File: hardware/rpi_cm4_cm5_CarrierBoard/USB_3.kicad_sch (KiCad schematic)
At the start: 92 parts, among them J2 0484050003, J3 0484050003, U6 SST25VF512A, U7 UPD720202K8-711-BAA-A, U8 AP2192AFGEG-7, Y1 24MHz

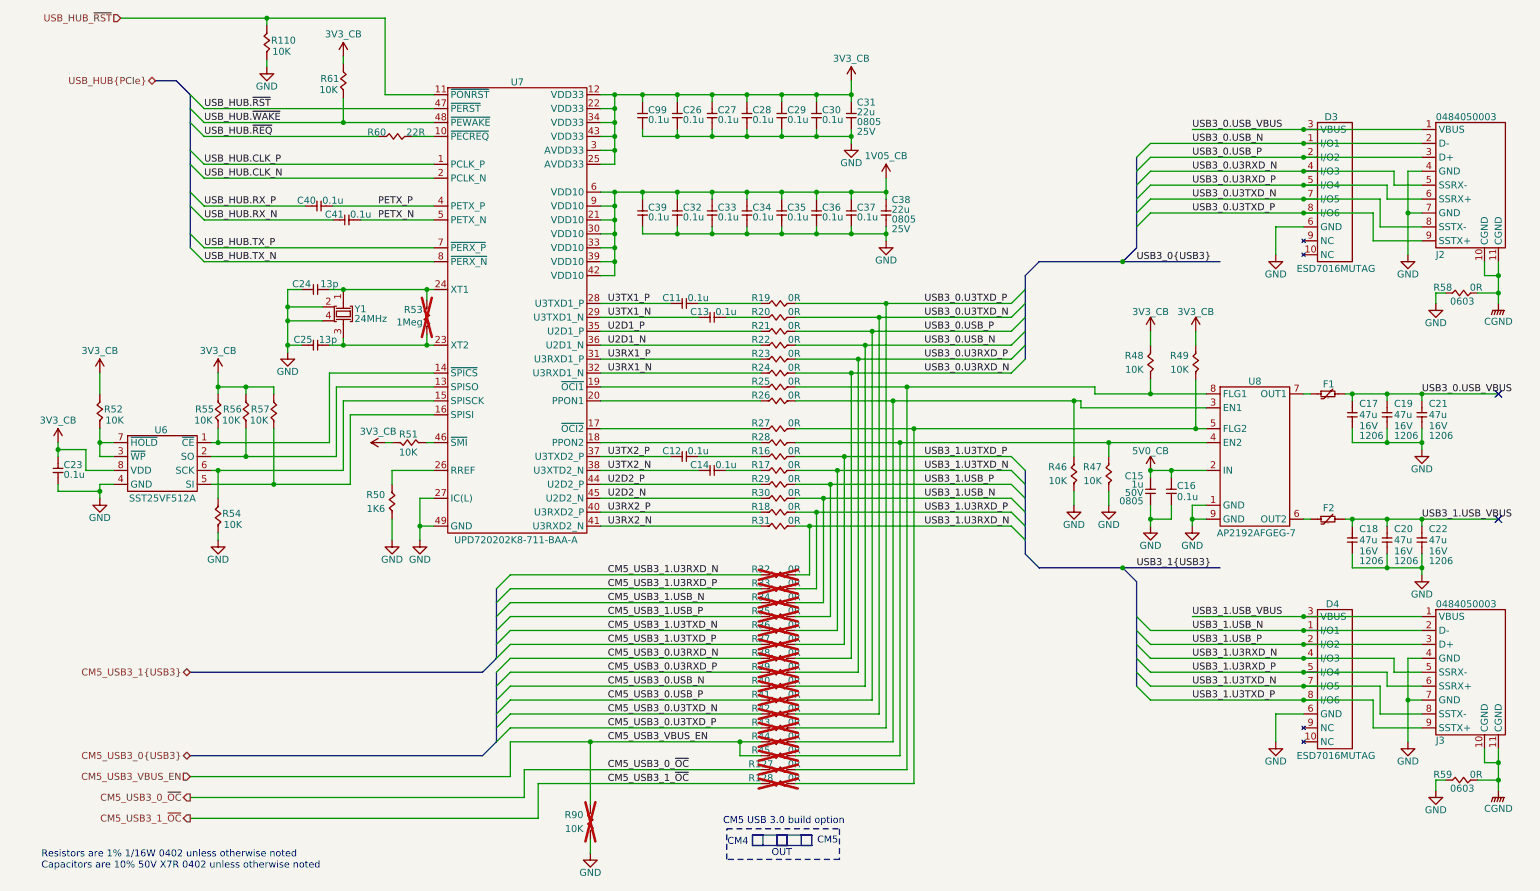
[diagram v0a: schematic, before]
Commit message: Add power-up and power kill sequences Modify schematics to add net classes for DiffPairs
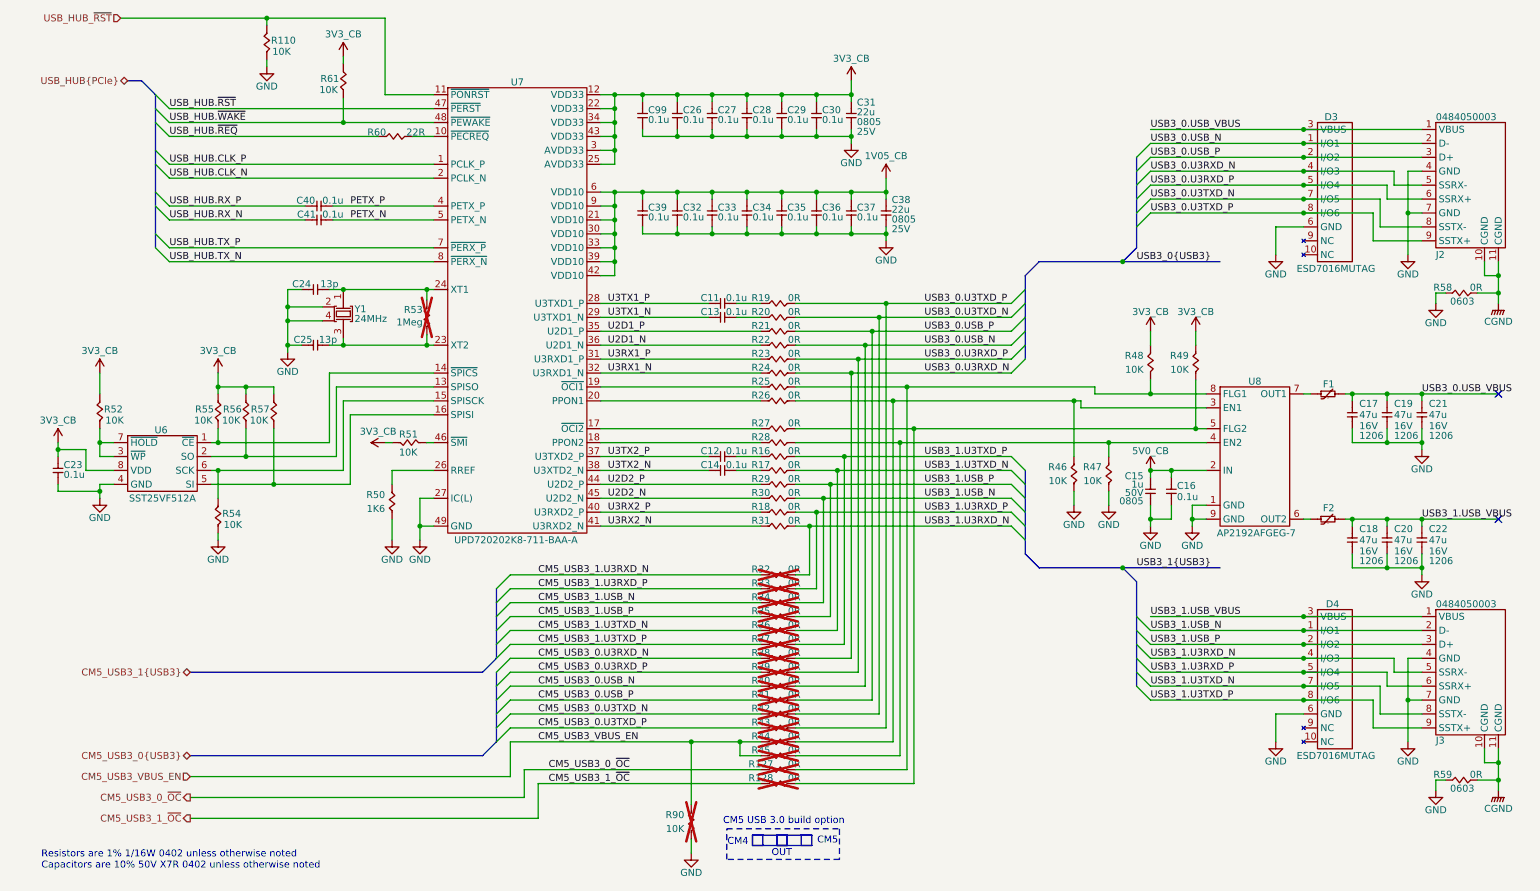
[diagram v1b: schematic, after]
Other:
- moved on the sheet: C11, C12, C13, C14, C41, R90

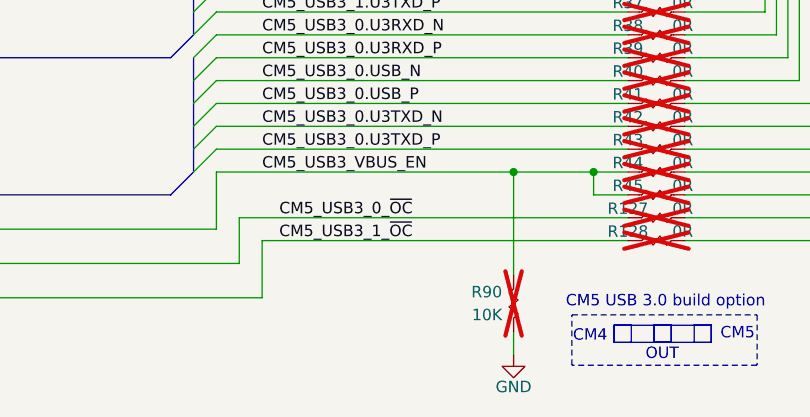
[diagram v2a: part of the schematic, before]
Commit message: Add preliminary BOM and preliminary .pdf schmematics Add BOM option for I2C control of ILI2132A for CapTouch HMI Add BOM options and DNP / 0R resistors for CM4 - CM5 build options
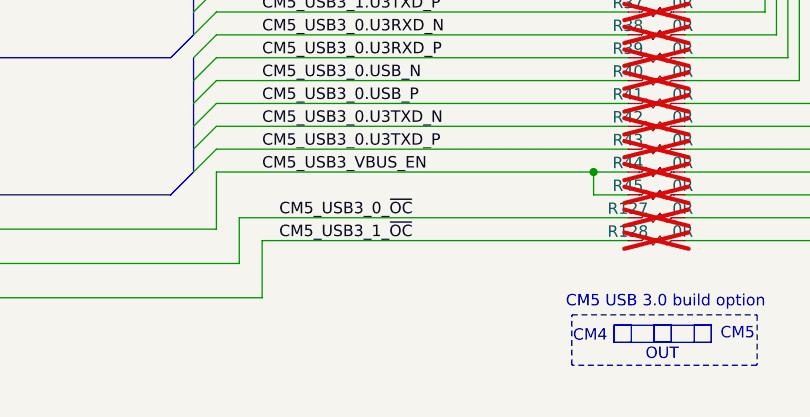
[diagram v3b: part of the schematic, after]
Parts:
- removed R90: 10K, footprint:RES_0402, symbol KicadCompDb:Resistors/RES_SMT_00013

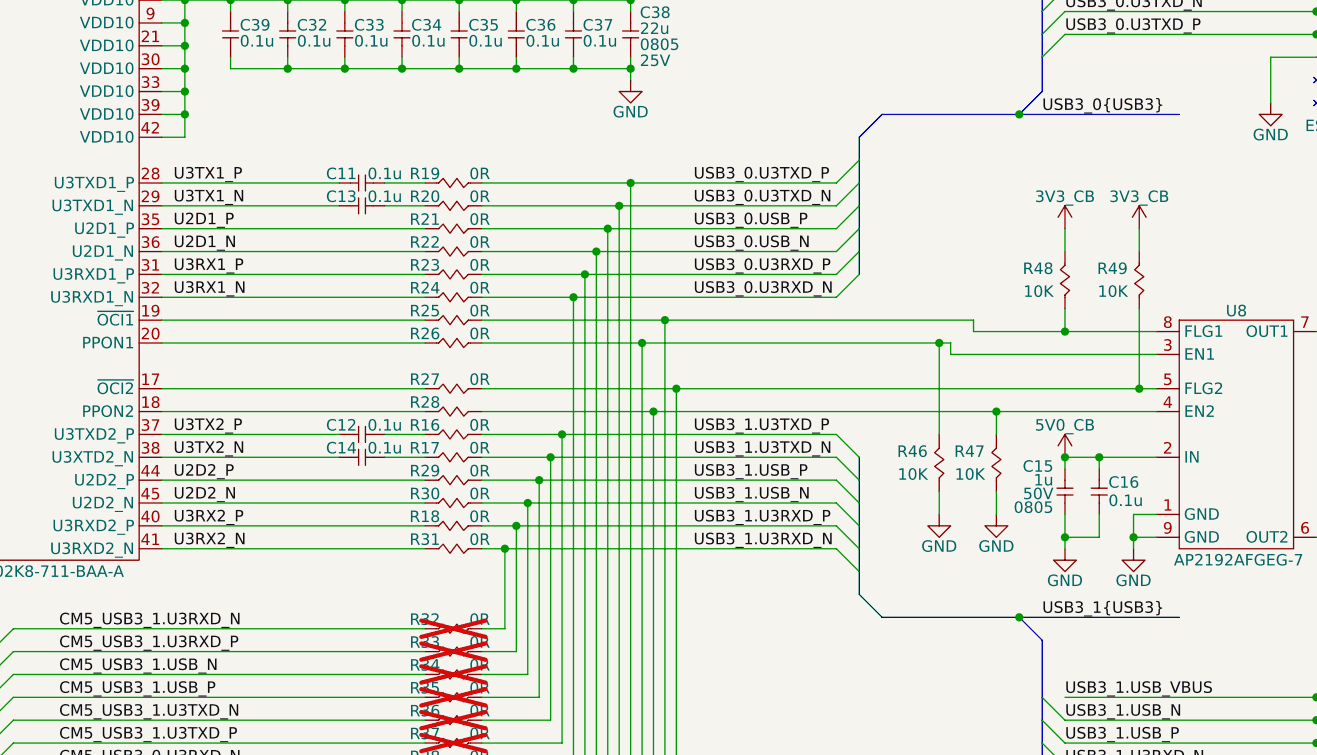
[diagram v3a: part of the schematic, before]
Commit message: Update watchdog timer circuit to add external watchdog timer IC to be fed by PIC Adjust reset scheme in power supply sheet accordingly Adjust PinMux, regen BOM and PDF schematics (preliminary) Start preliminary component placement in the PCB
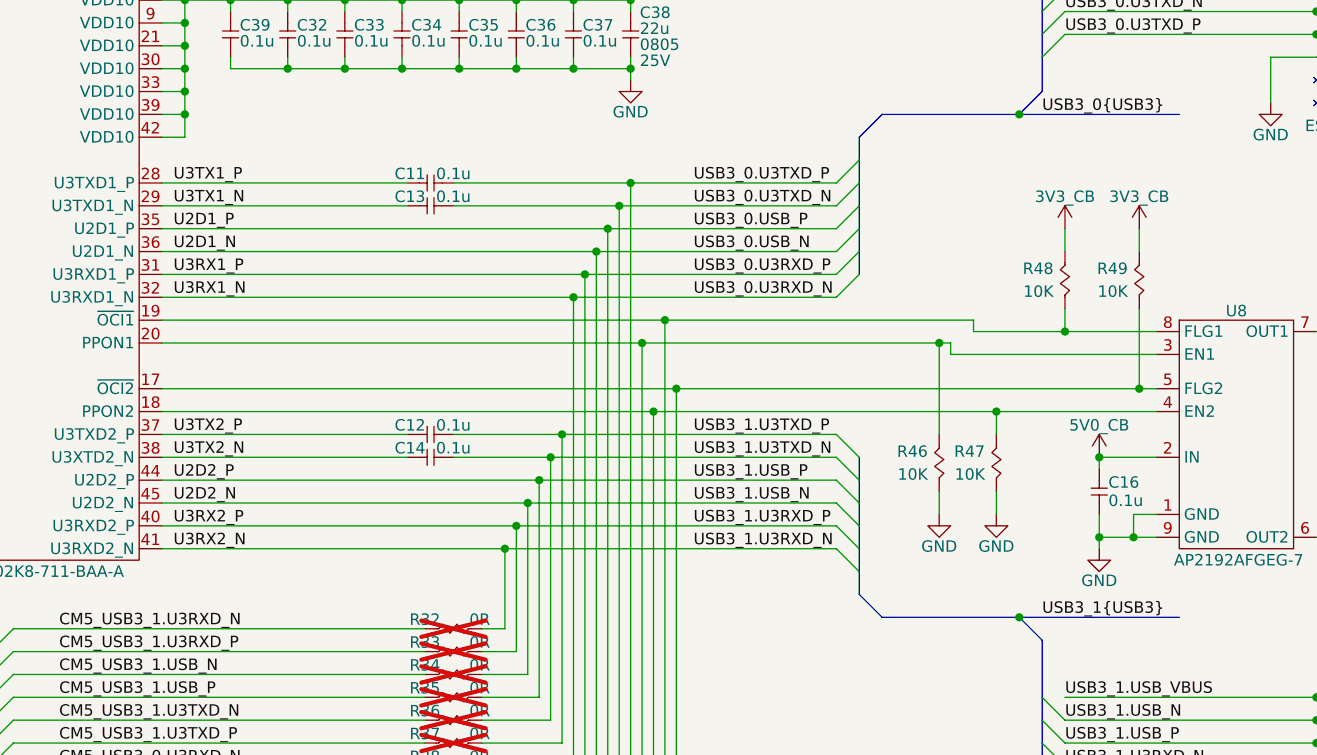
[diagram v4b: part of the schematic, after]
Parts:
- removed C15: 1u, footprint:CAP_NONPOL_0805, symbol KicadCompDb:Capacitors/CAP_CER_SMT_00002
- removed R16, R17, R18, R19, R20, R21, R22, R23, R24, R25, R26, R27, R28, R29, R30, R31: 0R, footprint:RES_0402, symbol KicadCompDb:Resistors/RES_SMT_00001
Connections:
- net USB3_0.U3RXD_N is gone; now on net U3RX1_N: D3.4 (I/O3), J2.5 (SSRX-), R38.2
- net USB3_0.U3RXD_P is gone; now on net U3RX1_P: D3.5 (I/O4), J2.6 (SSRX+), R39.2
- net USB3_0.USB_N is gone; now on net U2D1_N: D3.1 (I/O1), J2.2 (D-), R40.2
- net USB3_0.USB_P is gone; now on net U2D1_P: D3.2 (I/O2), J2.3 (D+), R41.2
- net USB3_1.U3RXD_N is gone; now on net U3RX2_N: D4.4 (I/O3), J3.5 (SSRX-), R32.2
- net USB3_1.U3RXD_P is gone; now on net U3RX2_P: D4.5 (I/O4), J3.6 (SSRX+), R33.2
- net USB3_1.USB_N is gone; now on net U2D2_N: D4.1 (I/O1), J3.2 (D-), R34.2
- net USB3_1.USB_P is gone; now on net U2D2_P: D4.2 (I/O2), J3.3 (D+), R35.2
- net USB3_0.U3TXD_N: now also C13.2
- net USB3_0.U3TXD_P: now also C11.2
- net USB3_1.U3TXD_N: now also C14.2
- net USB3_1.U3TXD_P: now also C12.2
- net at U7.17 (~{OCI2}): now also R128.2, R49.1, U8.5 (FLG2)
- net at R44.2, R46.2, U8.3 (EN1): now also U7.20 (PPON1)
- net at R45.2, R47.2, U8.4 (EN2): now also U7.18 (PPON2)
- net at R127.2, R48.1, U8.8 (FLG1): now also U7.19 (~{OCI1})
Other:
- moved on the sheet: C11, C12, C13, C14

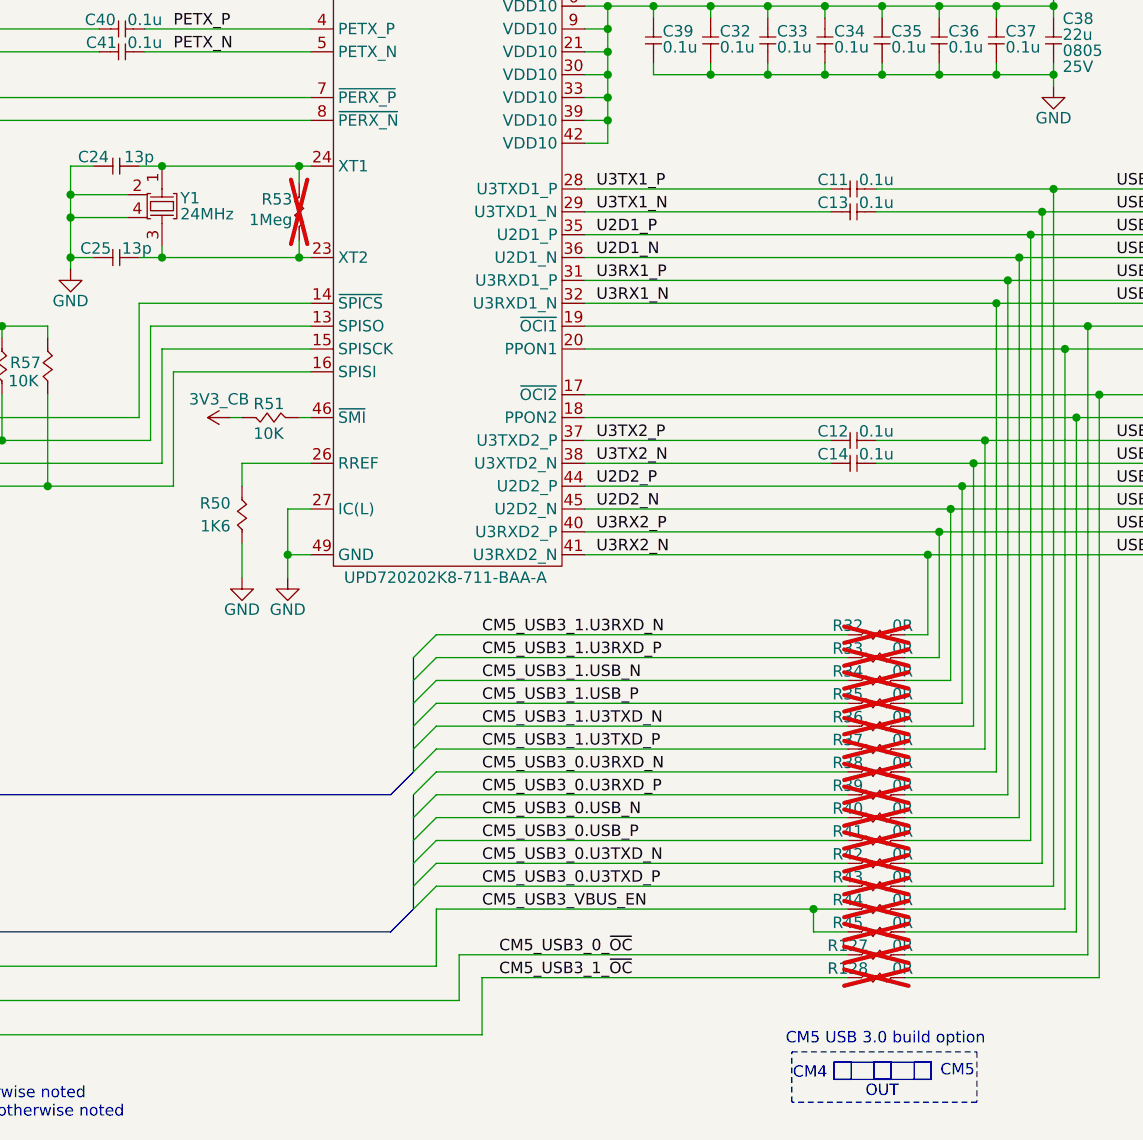
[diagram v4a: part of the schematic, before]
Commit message: Update preliminary placement, update DNP, regen BOM + Preliminary schematics
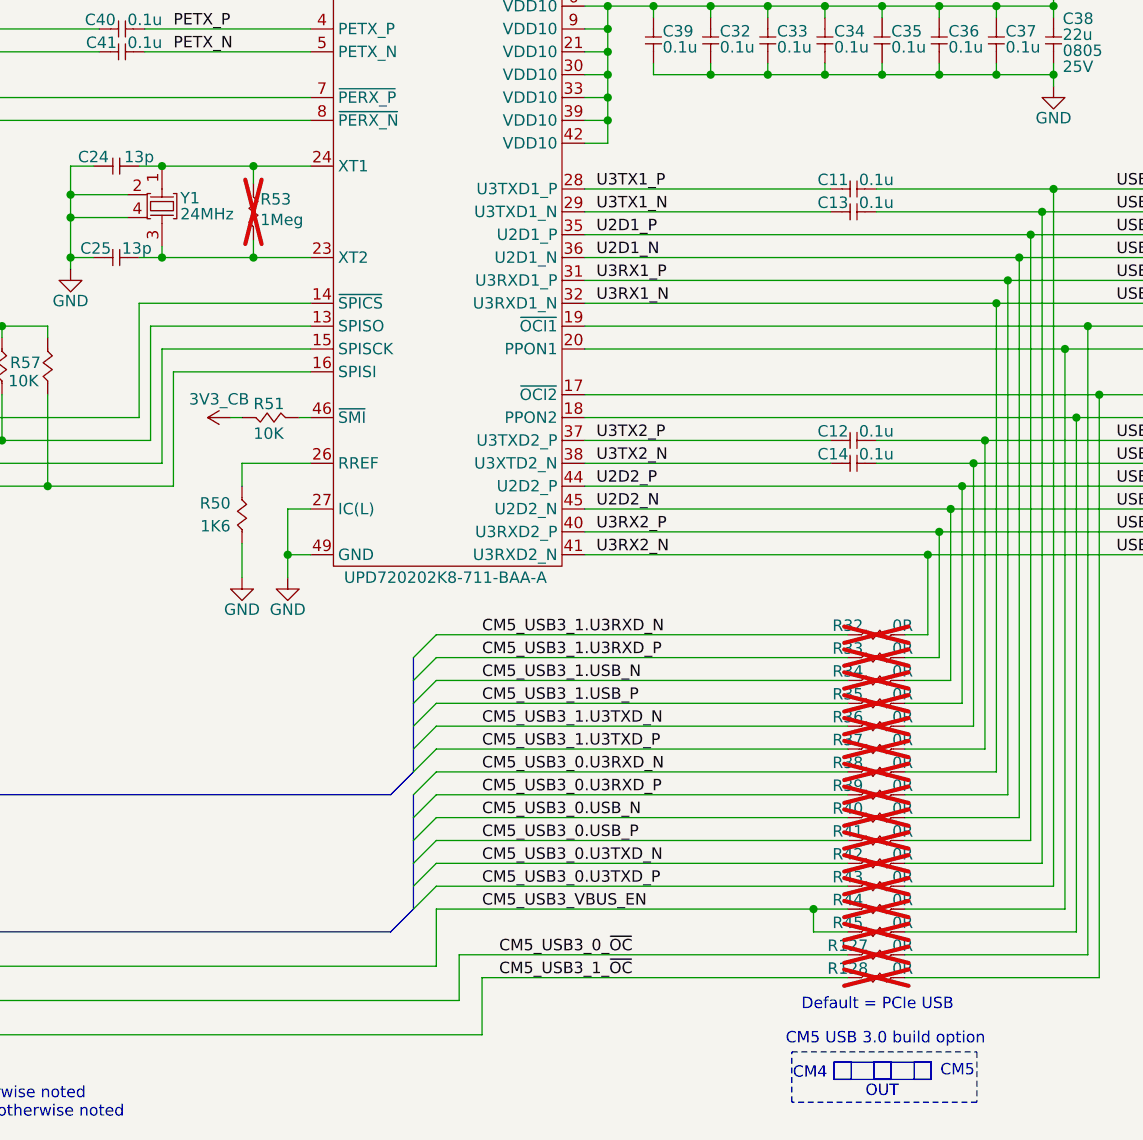
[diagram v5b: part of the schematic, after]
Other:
- note added: "Default = PCIe USB"
- moved on the sheet: R53
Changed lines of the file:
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@@
 		)
 	)
+	(text "Default = PCIe USB"
+		(exclude_from_sim no)
+		(at 148.082 159.258 0)
+		(effects
+			(font
+				(size 1.27 1.27)
+				(color 255 153 0 1)
+			)
+		)
+	)
 	(text "CM4"
 		(exclude_from_sim no)
@@
 	)
 	(junction
+		(at 78.74 66.04)
+		(diameter 0)
+		(color 0 0 0 0)
+	)
+	(junction
 		(at 161.29 38.1)
 		(diameter 0)
@@
 	)
 	(junction
-		(at 83.82 66.04)
-		(diameter 0)
-		(color 0 0 0 0)
-	)
-	(junction
-		(at 83.82 76.2)
-		(diameter 0)
-		(color 0 0 0 0)
-	)
-	(junction
 		(at 265.43 85.09)
 		(diameter 0)
@@
 	)
 	(junction
+		(at 78.74 76.2)
+		(diameter 0)
+		(color 0 0 0 0)
+	)
+	(junction
 		(at 219.71 99.06)
 		(diameter 0)
@@
 	(wire
 		(pts
+			(xy 78.74 66.04) (xy 85.09 66.04)
+		)
+		(stroke
+			(width 0)
+			(type default)
+		)
+	)
+	(wire
+		(pts
 			(xy 156.21 104.14) (xy 190.5 104.14)
 		)
@@
 	(wire
 		(pts
-			(xy 68.58 66.04) (xy 83.82 66.04)
+			(xy 68.58 66.04) (xy 78.74 66.04)
 		)
 		(stroke
@@
 	(wire
 		(pts
-			(xy 68.58 76.2) (xy 83.82 76.2)
+			(xy 68.58 76.2) (xy 78.74 76.2)
 		)
 		(stroke
@@
 	(wire
 		(pts
-			(xy 83.82 66.04) (xy 85.09 66.04)
-		)
-		(stroke
-			(width 0)
-			(type default)
-		)
-	)
-	(wire
-		(pts
 			(xy 99.06 146.05) (xy 144.78 146.05)
 		)
@@
 	(wire
 		(pts
-			(xy 83.82 76.2) (xy 85.09 76.2)
-		)
-		(stroke
-			(width 0)
-			(type default)
-		)
-	)
-	(wire
-		(pts
 			(xy 82.55 104.14) (xy 85.09 104.14)
 		)
@@
 	(wire
 		(pts
-			(xy 83.82 74.295) (xy 83.82 76.2)
+			(xy 78.74 74.295) (xy 78.74 76.2)
 		)
 		(stroke
@@
 	(wire
 		(pts
-			(xy 83.82 66.04) (xy 83.82 67.945)
+			(xy 78.74 66.04) (xy 78.74 67.945)
 		)
 		(stroke
@@
 	(wire
 		(pts
+			(xy 78.74 76.2) (xy 85.09 76.2)
+		)
+		(stroke
+			(width 0)
+			(type default)
+		)
+	)
+	(wire
+		(pts
 			(xy 223.52 105.41) (xy 223.52 107.95)
 		)
@@
 	(symbol
 		(lib_id "KicadCompDb:Resistors/RES_SMT_00006")
-		(at 83.82 73.025 270)
-		(mirror x)
+		(at 78.74 73.025 90)
 		(unit 1)
 		(exclude_from_sim no)
@@
 		(dnp yes)
 		(property "Reference" "R53"
-			(at 83.058 69.723 90)
+			(at 79.502 69.723 90)
 			(effects
 				(font
@@
 		)
 		(property "Value" "1Meg"
-			(at 83.058 72.009 90)
+			(at 79.502 72.009 90)
 			(effects
 				(font
@@
 		)
 		(property "Footprint" "footprint:RES_0402"
-			(at 61.722 72.517 0)
+			(at 100.838 72.517 0)
 			(effects
 				(font
@@
 		)
 		(property "Datasheet" "https://www.yageogroup.com/content/datasheet/asset/file/PYU-RC_GROUP_51_ROHS_L"
-			(at 83.82 73.025 0)
+			(at 78.74 73.025 0)
 			(effects
 				(font
@@
 		)
 		(property "Description" "RES 1M OHM 1% 1/16W 0402"
-			(at 73.914 71.247 0)
+			(at 88.646 71.247 0)
 			(effects
 				(font
@@
 		)
 		(property "Tolerance" "1%"
-			(at 63.5 72.771 0)
+			(at 99.06 72.771 0)
 			(effects
 				(font
@@
 		)
 		(property "Power" "1/16W"
-			(at 69.596 72.771 0)
+			(at 92.964 72.771 0)
 			(effects
 				(font
@@
 		)
 		(property "Package" "0402"
-			(at 67.564 73.025 0)
+			(at 94.996 73.025 0)
 			(effects
 				(font
@@
 		)
 		(property "Manufacturer" "YAGEO"
-			(at 65.532 72.771 0)
+			(at 97.028 72.771 0)
 			(effects
 				(font
@@
 		)
 		(property "Manufacturer Part Number" "RC0402FR-131ML"
-			(at 75.946 72.771 0)
+			(at 86.614 72.771 0)
 			(effects
 				(font
@@
 		)
 		(property "Distributor" "DigiKey"
-			(at 77.978 73.025 0)
+			(at 84.582 73.025 0)
 			(effects
 				(font
@@
 		)
 		(property "Distributor Part Number" "13-RC0402FR-131MLCT-ND"
-			(at 71.628 72.263 0)
+			(at 90.932 72.263 0)
 			(effects
 				(font
@@
 		)
 		(property "Temperature Coefficient" "±100ppm/°C"
-			(at 83.82 73.025 0)
+			(at 78.74 73.025 0)
 			(effects
 				(font
@@
 		)
 		(property "Operating Temperature" "-55°C ~ 155°C"
-			(at 59.436 72.263 0)
+			(at 103.124 72.263 0)
 			(effects
 				(font
@@
 		)
 		(property "Type" "RES SMT"
-			(at 83.82 73.025 0)
+			(at 78.74 73.025 0)
 			(show_name yes)
 			(effects
@@
 		)
 		(property "Dimensions" "1.00mm x 0.50mm"
-			(at 83.82 73.025 0)
+			(at 78.74 73.025 0)
 			(show_name yes)
 			(effects
